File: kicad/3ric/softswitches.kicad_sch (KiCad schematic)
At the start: 34 parts

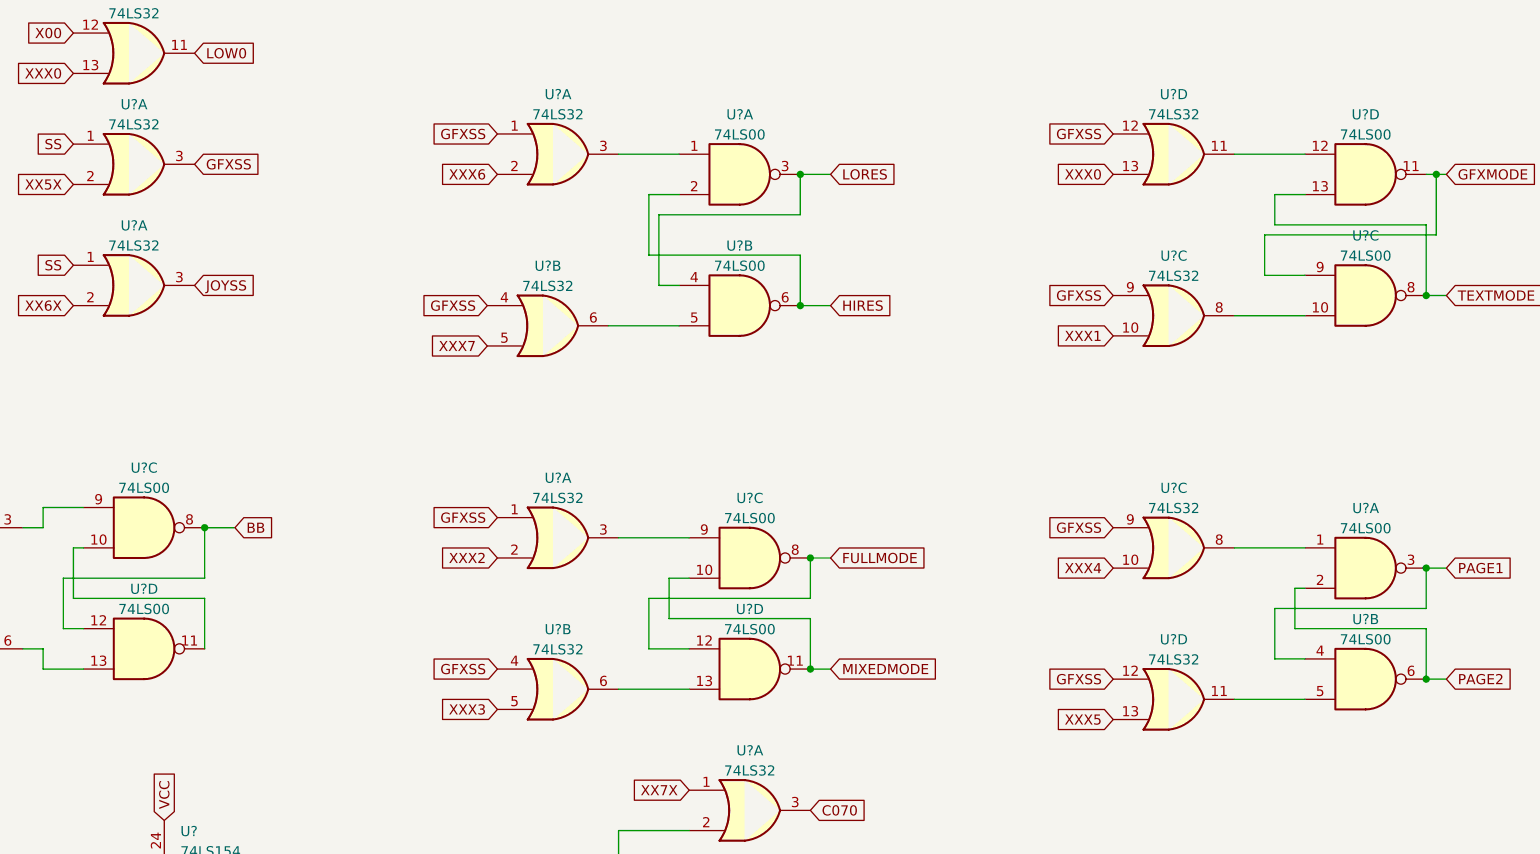
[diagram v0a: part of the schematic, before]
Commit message: upgraded to kicad 8, updates to schematic - added snes controllers, mouse port, many fixes
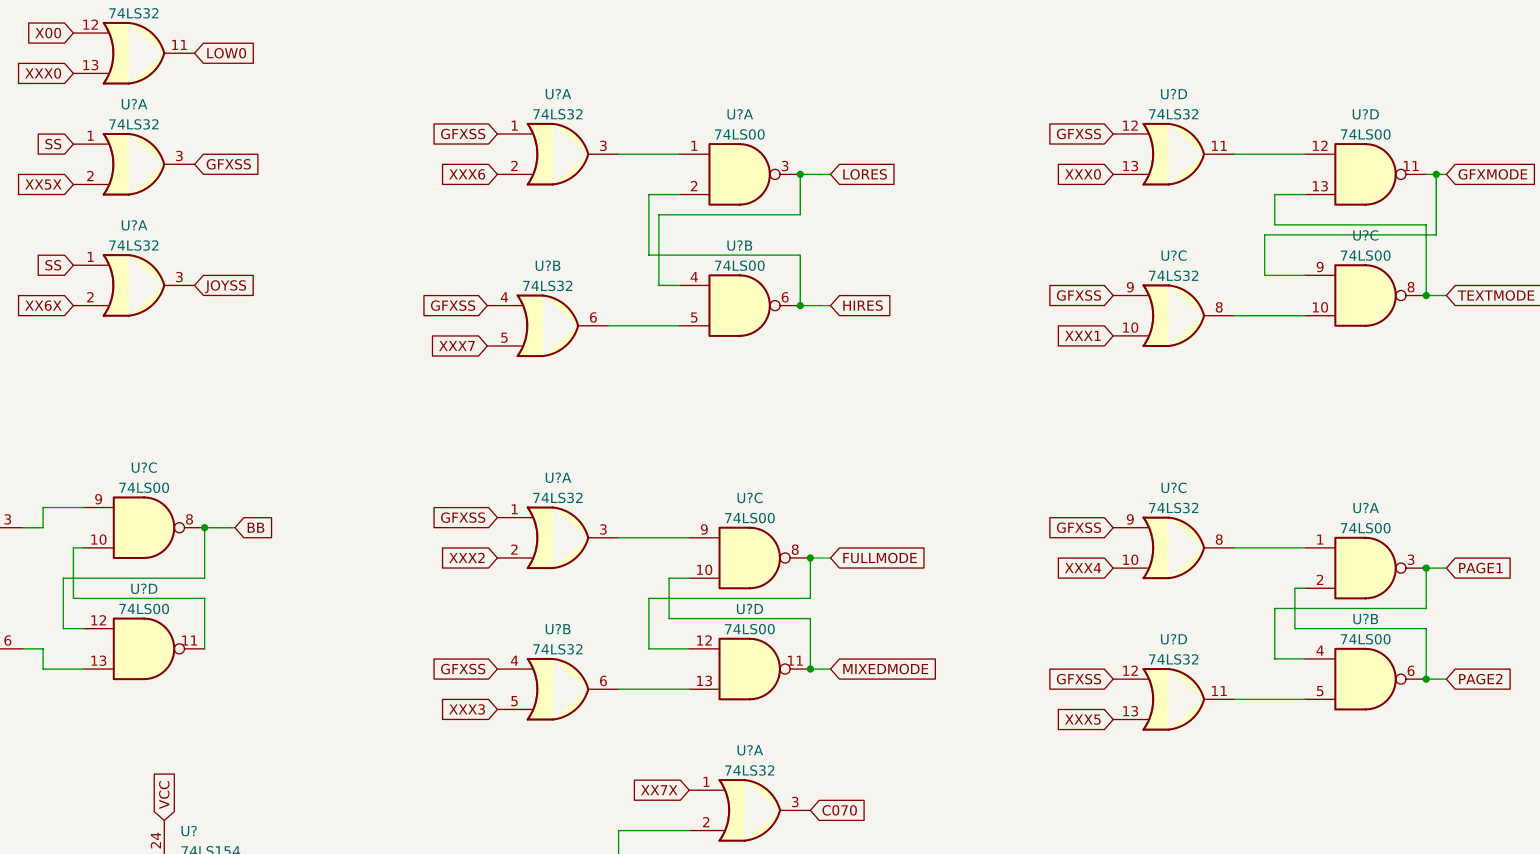
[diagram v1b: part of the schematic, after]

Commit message: schematic updates
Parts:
- added U2: 74LS32, symbol 74xx:74LS32
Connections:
- net SS: now also U2.4
- net XXEX: now reaches U?.16 (S14)
- net XXEX: now also U2.5
- new net DISKSS: U2.6
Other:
- moved on the sheet: U?A, U?D

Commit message: picking up steam on the layout - lots of progress
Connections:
- net !PHI2: now also U?.19 (E1), U?.19 (E1)
- net GND: no longer U?.19 (E1), U?.19 (E1)

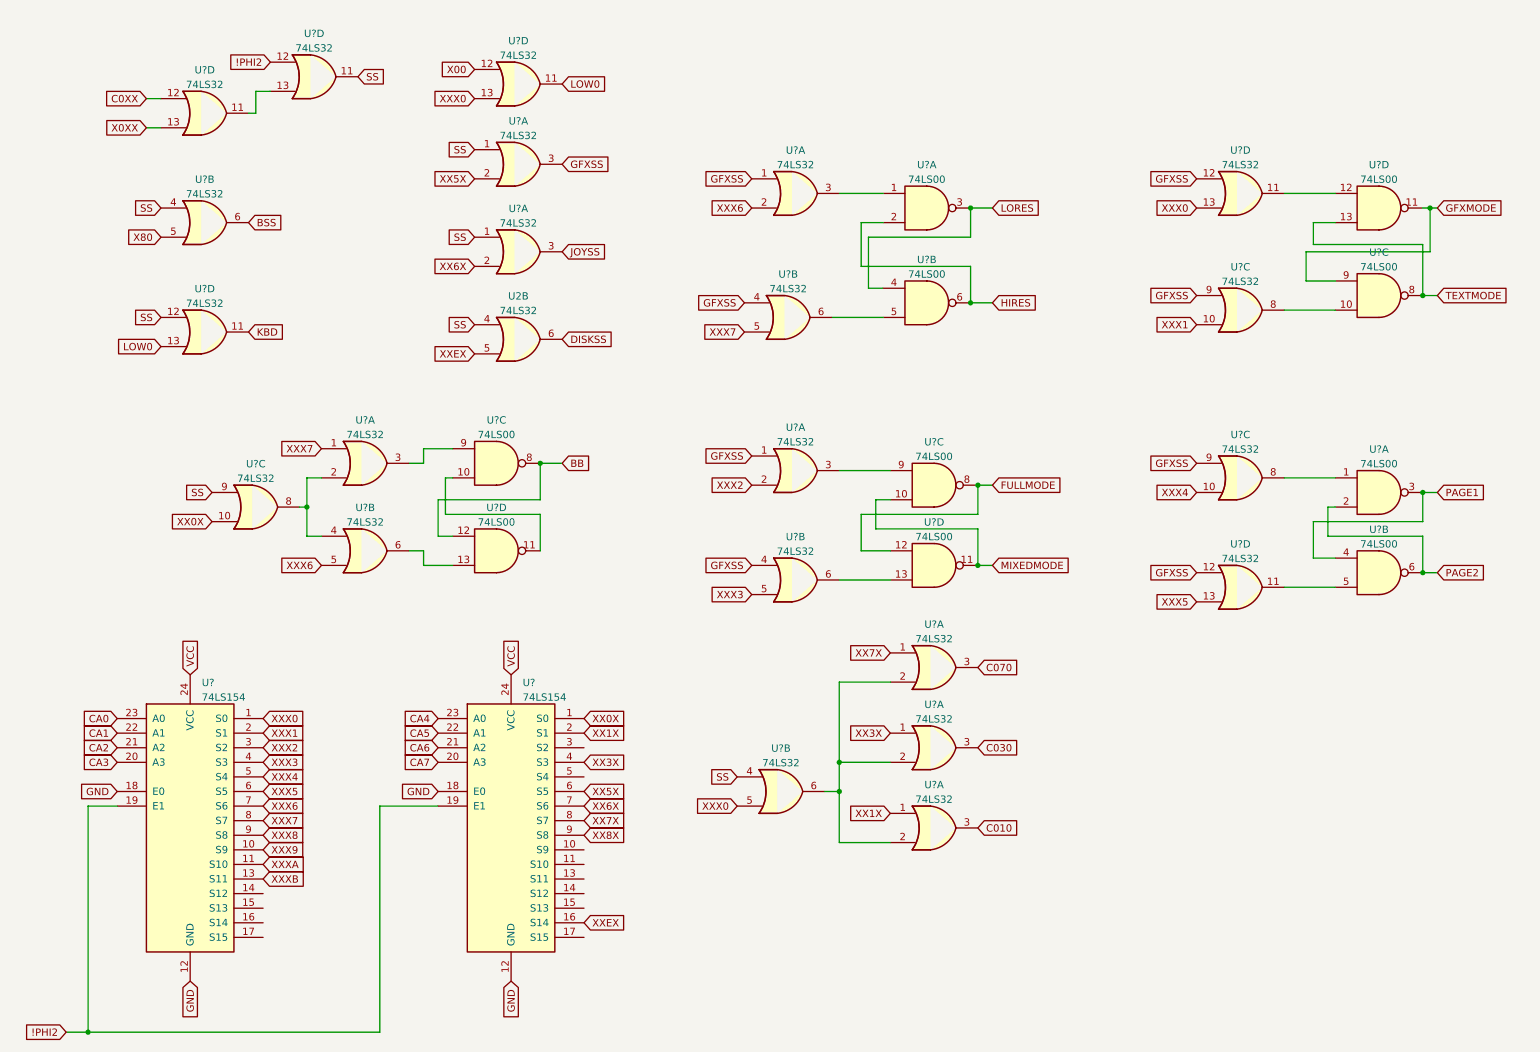
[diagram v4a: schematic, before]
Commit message: update units for soft switch logic to match breadboard
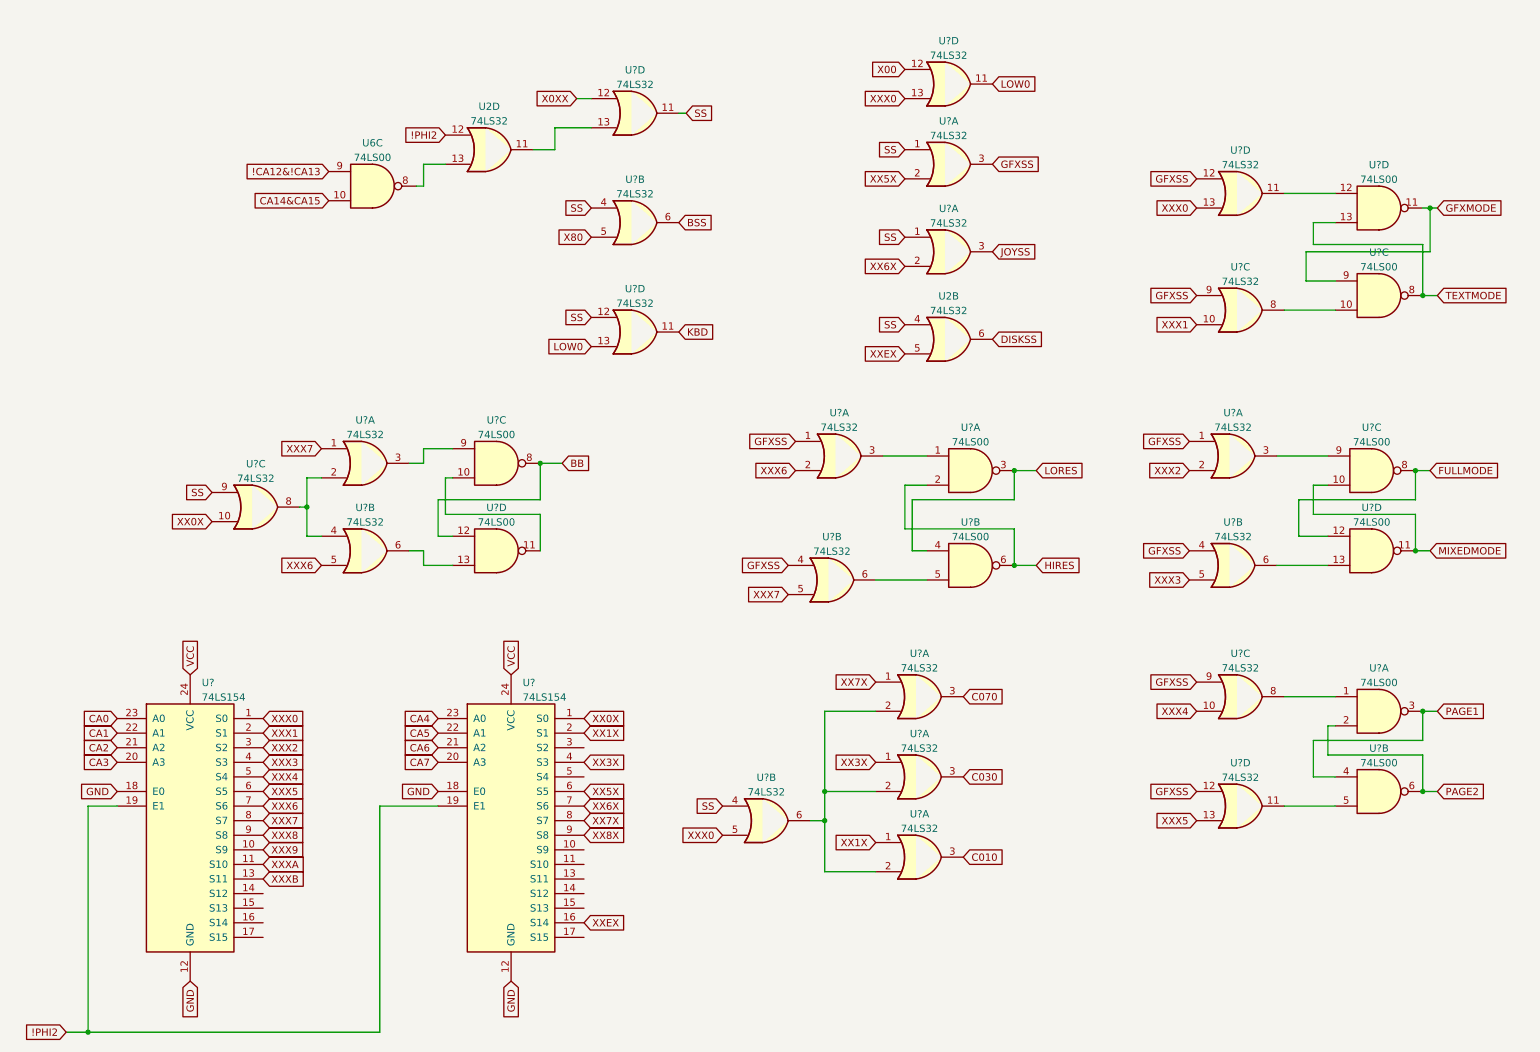
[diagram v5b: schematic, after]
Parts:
- removed U?: 74LS32, symbol 74xx:74LS32
- added unit 4 of U2
- added U6: 74LS00, symbol 74xx:74LS00
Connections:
- net C0XX is gone; now on net X0XX: U?.12
- net !PHI2: now also U2.12
- net SS: now also U?.11
- net X0XX: no longer U?.13
- new net: U2.13, U6.8
- new net: U2.11, U?.13
- new net !CA12&!CA13: U6.9
- new net CA14&CA15: U6.10
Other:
- moved on the sheet: U2B, U?A, U?B, U?C, U?D

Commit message: update schematic based on breadboard
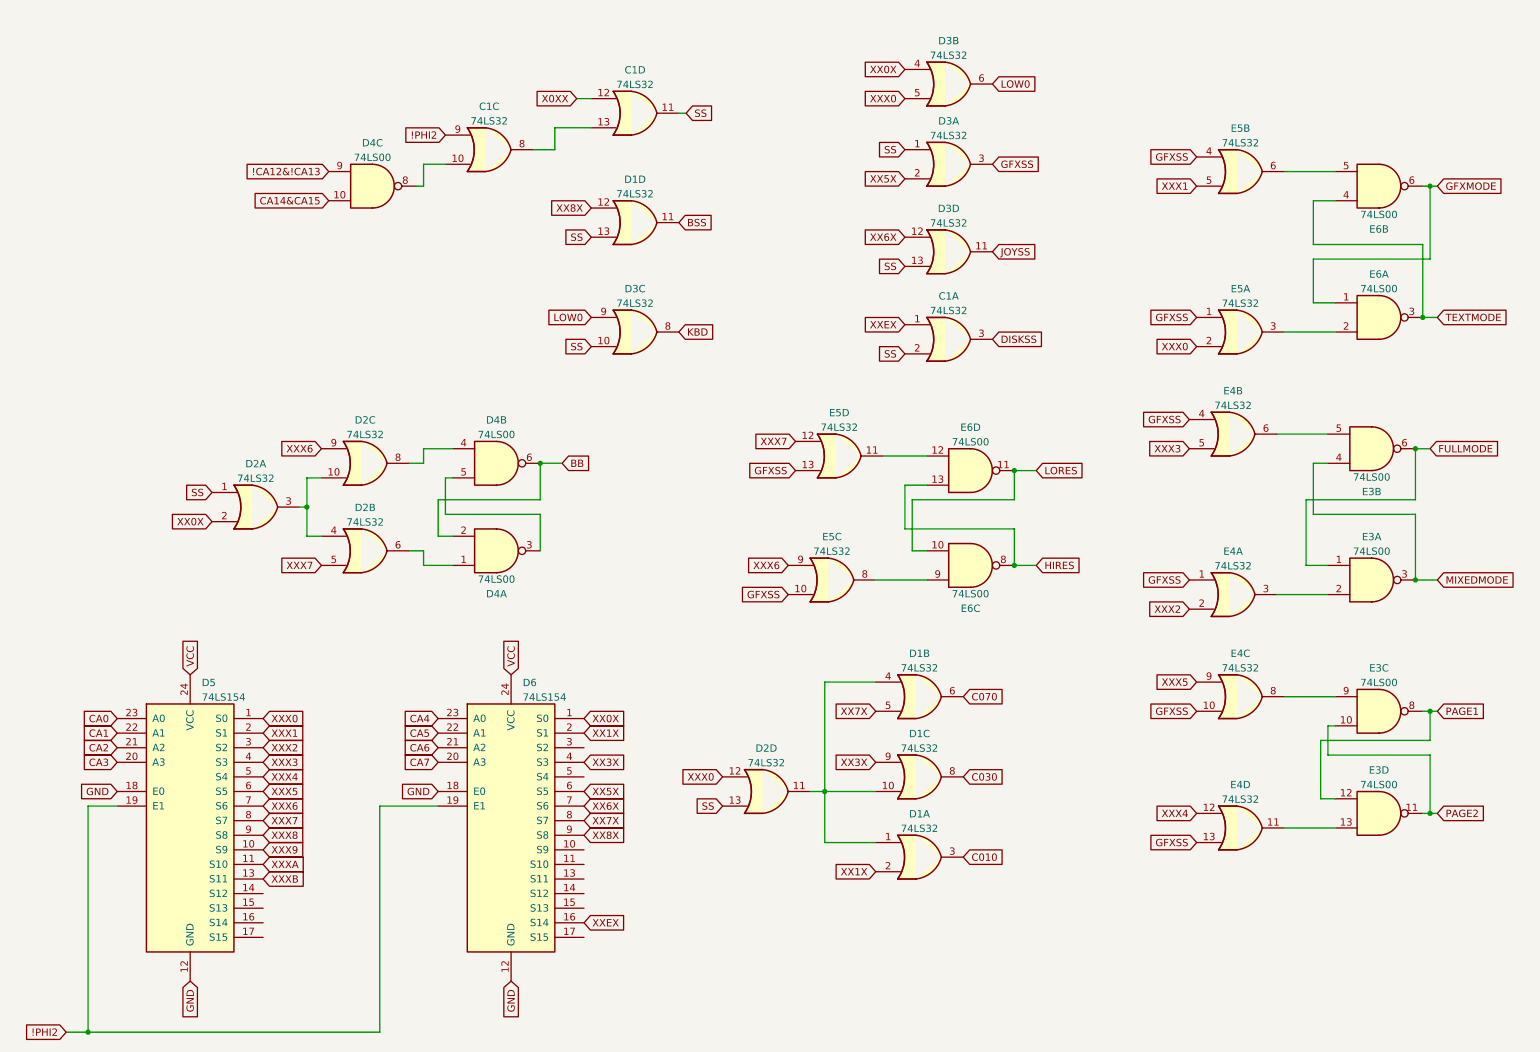
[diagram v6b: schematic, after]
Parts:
- gave numbers to parts that had none: 11
- renumbered U2 to C1, U6 to D4
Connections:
- net !PHI2: now also C1.9; no longer C1.12
- net BB: now also D4.2, D4.6; no longer D4.12, D4.8
- net BSS: now also D1.11; no longer D1.6
- net C030: now also D1.8; no longer D1.3
- net C070: now also D1.6; no longer D1.3
- net DISKSS: now also C1.3; no longer C1.6
- net FULLMODE: now also E3.1, E3.6; no longer E3.12, E3.8
- net GFXMODE: now also E6.1, E6.6; no longer E6.11, E6.9
- net GFXSS: now also E4.1, E4.10, E4.13, E4.4, E5.1, E5.10, E5.13, E5.4; no longer E4.1, E4.12, E4.4, E4.9, E5.1, E5.12, E5.4, E5.9
- net HIRES: now also E6.13, E6.8; no longer E6.2, E6.6
- net JOYSS: now also D3.11; no longer D3.3
- net KBD: now also D3.8; no longer D3.11
- net LORES: now also E6.10, E6.11; no longer E6.3, E6.4
- net LOW0: now also D3.6, D3.9; no longer D3.11, D3.13
- net MIXEDMODE: now also E3.3, E3.4; no longer E3.10, E3.11
- net PAGE1: now also E3.12, E3.8; no longer E3.3, E3.4
- net PAGE2: now also E3.10, E3.11; no longer E3.2, E3.6
- net SS: now also C1.2, D1.13, D2.1, D2.13, D3.10, D3.13; no longer C1.4, D1.4, D2.4, D2.9, D3.1, D3.12
- net TEXTMODE: now also E6.3, E6.4; no longer E6.13, E6.8
- net XX0X: now also D2.2, D3.4; no longer D2.10
- net XX1X: now also D1.2; no longer D1.1
- net XX3X: now also D1.9; no longer D1.1
- net XX6X: now also D3.12; no longer D3.2
- net XX7X: now also D1.5; no longer D1.1
- net XX8X: now also D1.12
- net XXEX: now also C1.1; no longer C1.5
- net XXX0: now also D2.12, D3.5, E5.2; no longer D2.5, D3.13, E5.13
- net XXX1: now also E5.5; no longer E5.10
- net XXX2: now also E4.2; no longer E4.2
- net XXX3: now also E4.5; no longer E4.5
- net XXX4: now also E4.12; no longer E4.10
- net XXX5: now also E4.9; no longer E4.13
- net XXX6: now also D2.9, E5.9; no longer D2.5, E5.2
- net XXX7: now also D2.5, E5.12; no longer D2.1, E5.5
- net at E4.11: now also E3.13; no longer E3.5
- net at D4.8: now also C1.10; no longer C1.13
- net at E4.8: now also E3.9; no longer E3.1
- net at C1.13: now also C1.8; no longer C1.11
- net at D2.6: now also D4.1; no longer D4.13
- removed net X00: D3.12
- removed net X80: D1.5
- new net: D2.10, D2.3, D2.4
- new net: D2.8, D4.4
- new net: E3.5, E4.6
- new net: D4.3, D4.5
- new net: E5.6, E6.5
- new net: E3.2, E4.3
- new net: E5.11, E6.12
- new net: D1.1, D1.10, D1.4, D2.11
- new net: E5.8, E6.9
- new net: E5.3, E6.2
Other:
- moved on the sheet: D2D, E3A, E3B, E3D, E4A, E4B, E4D, E5A, E5B, E6A, E6B
